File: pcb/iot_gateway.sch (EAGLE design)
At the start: 183 parts, among them CON1 LiPo Battery, J2 DC-JACK, Q1 AO3401, Q2 AO3401, Q3 AO3400, Q4 AO3400, T1 BC817-25, T2 BC817-25, T3 BC817-25, T4 BC817-25, T5 BC817-25, U1 EFM32GG11B4XX_Q100, U10 CCS811, U11 MIC4682, U12 MIC4682, U13 MIC39101, U14 FS312F-G, U15 TP4056, U16 FS8205, U17 ER-TFT035-6, U2 SST26VF064B, U3 SST26VF016B, U4 ESP8266EX, U5 RFM69HW, U6 SIM800C, U7 SI7021, U8 SI7210, U9 BMP280, X1 BM06B-SRSS-TB, X2 BM06B-SRSS-TB, Y1 8 MHz, Y2 32.768 kHz, Y3 24 MHz

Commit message: Change libs to new scheme
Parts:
- removed A1, A2, A3, A4: U.FL, SparkFun:U.FL
- removed J1: (no value), SparkFun-Connectors:SIMHOLDERSIM
- removed X1, X2: BM06B-SRSS-TB, con-jst2:BM06B-SRSS-TB
- added CON2: 6P-SH-TOP, JST:6P-SH-TOP
- added CON3: 2P-PH-TOP, JST:2P-PH-TOP
- added RFCON1, RFCON2, RFCON3, RFCON4: RFCON-U.FL, RF Connector:RFCON-U.FL
- added SIM1: SIMHOLDER-SMD, SIM Holder:SIMHOLDER-SMD
- B1: value KLJ-1230 -> BUZZER-SMD; device muRata-piezo:PKLCS1212E2400-R1 -> Buzzer:BUZZER-SMD
- C1, C13, C14, C15, C16, C2, C21, C23, C28, C29, C3, C30, C31, C37, C38, C4, C43, C47, C49, C5, C50, C52, C53, C54, C6, C7: device Kemet_by_JSilva:C0603C104K4RACTU -> Capacitor:CAPACITOR-0603
- C10, C11, C9: device Kemet_by_JSilva:C0603C102J5GACTU -> Capacitor:CAPACITOR-0603
- C12, C22, C36, C42, C46, C48, C51: device SparkFun:CAP_POL1206-KIT -> Capacitor:TANTALUM-CAPACITOR-CASE-A-EIA3216
- C17: device Kemet_by_JSilva:C0603C100J5GACTU -> Capacitor:CAPACITOR-0603
- C18: device Kemet_by_JSilva:C0603C479C5GACTU -> Capacitor:CAPACITOR-0603
- C19, C20: device Kemet_by_JSilva:C0603C200J5GACTU -> Capacitor:CAPACITOR-0603
- C24: device Kemet_by_JSilva:C1206C107M9PACTU -> Capacitor:CAPACITOR-0603
- C25, C8: device Kemet_by_JSilva:C0603C105K9RACTU -> Capacitor:CAPACITOR-0603
- C26, C27: device Kemet_by_JSilva:C0603C330J5GACTU -> Capacitor:CAPACITOR-0603
- C32, C33: device Kemet_by_JSilva:C0603X104K5RACTU -> Capacitor:CAPACITOR-0603
- C34: value 470UF -> 470uF; device Panasonic-EEE0_EEE1_EEE2_EEEFC:EEE-1CA471UAP-CASE-F -> Capacitor:ALUMINIUM-CAPACITOR-CASE-F
- C35, C41, C44, C45: device Kemet_by_JSilva:C0603C471J5GACTU -> Capacitor:CAPACITOR-0603
- C39, C40: value 220UF -> 220uF; device Panasonic-EEE0_EEE1_EEE2_EEEFC:EEE-0JA221WP-CASE-D -> Capacitor:ALUMINIUM-CAPACITOR-CASE-D
- CON1: value LiPo Battery -> 6P-SH-TOP; device JST_PH_SMD:JST_PH_SMD_2 -> JST:6P-SH-TOP; MF JST (JAPAN SOLDERLESS TERMINALS) -> (none); MPN B2B-PH-SM4-TB(LF)(SN) -> (none); OC_NEWARK unknown -> (none)
- D1: device SparkFun-LED:WS2812B -> LED:WS2812B-SMD
- D2: device ATWINC1500:LED1206 -> LED:LED1206
- D3: device smaj_10:SMAJ12A -> TVS:SMAJ12A
- D4, D5: device diodes:SK54L -> Generic Diode:SK54L
- D6, D7: device diodes:DSK24 -> Generic Diode:DSK24
- E1, E2: value ANTENNATRACE-15.2MM -> 2.4GHZTRACE-15.2MM; device esp8266-development-board:ANTENNATRACE-15.2MM -> Microstrip Antenna:2.4GHZTRACE-15.2MM
- J2: value DC-JACK -> DCJACK-SMD; device dc-jack-smd:DC-JACK -> DC Jack:DCJACK-SMD
- L1: device microbuilder 2:INDUCTOR0603 -> Inductor:INDUCTOR-0603
- L2, L3: device Inductor:SLH1207S680MTT -> Inductor:INDUCTOR-12X12X7MM
- R1, R17, R18, R2, R20, R21, R22, R24, R28, R31, R32, R33, R36, R37, R4, R40, R43, R50, R53, R6, R67, R7: device Vishay_by_JSilva:CRCW060310K0FKEA -> Resistor:RESISTOR-0603
- R10, R11, R9: device Vishay_by_JSilva:CRCW06031M00FKEA -> Resistor:RESISTOR-0603
- R12, R13, R14, R59: device Vishay_by_JSilva:CRCW0603100RFKEA -> Resistor:RESISTOR-0603
- R15, R25, R38, R41, R5, R51, R52, R54, R56, R57, R60, R61, R66, R8: device Vishay_by_JSilva:CRCW0603100KFKEA -> Resistor:RESISTOR-0603
- R16, R34, R35, R64, R65: device Vishay_by_JSilva:CRCW06030000Z0EA -> Resistor:RESISTOR-0603
- R19: device Vishay_by_JSilva:CRCW060312K0FKEA -> Resistor:RESISTOR-0603
- R23: device Vishay_by_JSilva:CRCW0603200RFKEA -> Resistor:RESISTOR-0603
- R26, R27, R29: device Vishay_by_JSilva:CRCW060322R0FKEA -> Resistor:RESISTOR-0603
- R3, R58, R68: device Vishay_by_JSilva:CRCW06031K00FKEA -> Resistor:RESISTOR-0603
- R30: device Vishay_by_JSilva:CRCW0603330RFKEA -> Resistor:RESISTOR-0603
- R39, R42, R63: device Vishay_by_JSilva:CRCW060310M0JNEA -> Resistor:RESISTOR-0603
- R44, R48: device Vishay_by_JSilva:CRCW06033K01FKEA -> Resistor:RESISTOR-0603
- R45: device Vishay_by_JSilva:CRCW0603953RFKEA -> Resistor:RESISTOR-0603
- R46: device Vishay_by_JSilva:CRCW0603300KFKEA -> Resistor:RESISTOR-0603
- R47, R55: device Vishay_by_JSilva:CRCW060347K0FKEA -> Resistor:RESISTOR-0603
- R49: device Vishay_by_JSilva:CRCW06031K20FKEA -> Resistor:RESISTOR-0603
- R62: device Vishay_by_JSilva:CRCW06031K50FKEA -> Resistor:RESISTOR-0603
- S1: device Switches:TAC_SWITCHSMD -> Switch:TAC_SWITCHSMD
- S2, S3, S4: device Switches:TAC_SWITCHSMD_4.5X4.5 -> Switch:TAC_SWITCHSMD_4.5X4.5
- T1, T2, T3, T4, T5: value BC817-25 -> BC817; device BC817:BC817-25 -> Generic BJT:BC817; MPN BC81725 -> (none); OC_NEWARK 04X5937 -> (none)
- TP1, TP2, TP3, TP4, TP5: value TPB1,27 -> TESTPOINT; device ReflowController:TPB1,27 -> PADs:TESTPOINT
- U14: device buckboost:FS312F-G -> Fortune:FS312F-G
- U16: device buckboost:FS8205 -> Fortune:FS8205
- U4: device ESP8266EX:ESP8266EX -> Espressif:ESP8266EX
- Y1, Y3: device crystal2:NX5032GA -> Crystal:CRYSTAL2-SMD-5X3
- Y2: device crystal2:CRYTALCM200S -> Crystal:CRYSTALCM2000S
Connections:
- net !RESET: now also CON1-2.S; no longer X1-2.S
- net !WIFI_RST: now also CON2-1.S; no longer X2-1.S
- net 3V3: now also B1.+, CON1-1.S; no longer B1.A, X1-1.S
- net 5V0: now also C40.+; no longer C40.1
- net GBAT: now also CON3-2.S; no longer CON1.2
- net GND: now also C34.-, C39.-, C40.-, CON1-6.S, CON2-6.S, RFCON1.GND, RFCON2.GND, RFCON3.GND, RFCON4.GND, SIM1.GND; no longer A1.GND@0, A1.GND@1, A2.GND@0, A2.GND@1, A3.GND@0, A3.GND@1, A4.GND@0, A4.GND@1, C34.2, C39.2, C40.2, J1.GND, X1-6.S, X2-6.S
- net N$10: now also RFCON1.SIGNAL; no longer A1.SIGNAL
- net N$18: now also SIM1.CLK; no longer J1.CLK
- net N$2: now also RFCON4.SIGNAL; no longer A4.SIGNAL
- net N$22: now also RFCON3.SIGNAL; no longer A3.SIGNAL
- net N$3: now also SIM1.RST; no longer J1.RST
- net N$35: now also B1.-; no longer B1.B
- net N$39: now also SIM1.DATA; no longer J1.I/O
- net N$43: now also C39.+; no longer C39.1
- net N$45: now also RFCON2.SIGNAL; no longer A2.SIGNAL
- net SIM_VDD: now also SIM1.VCC; no longer J1.VCC
- net SWCLK: now also CON1-3.S; no longer X1-3.S
- net SWDIO: now also CON1-4.S; no longer X1-4.S
- net SWO: now also CON1-5.S; no longer X1-5.S
- net VBAT: now also CON3-1.S; no longer CON1.1
- net VIN: now also C34.+; no longer C34.1
- net WIFI_BOOT: now also CON2-2.S; no longer X2-2.S
- net WIFI_RX_FW: now also CON2-4.S; no longer X2-4.S
- net WIFI_TX_DBG: now also CON2-5.S; no longer X2-5.S
- net WIFI_TX_FW: now also CON2-3.S; no longer X2-3.S
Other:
- note added: "Option 2: L1: 5.6pF capacitor C17: Do not place C18: Do not place"
- note removed: "Option 2: L2: 5.6pF capacitor C15: Do not place C21: Do not place"

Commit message: Update libraries
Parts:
- C24: device Capacitor:CAPACITOR-0603 -> Capacitor:CAPACITOR-1206
- D1: device LED:WS2812B-SMD -> LED:WS2812B-SMD5050
- D4, D5: OCLCSC C129854 -> C129816
- R28, R30, R31, R32, R33: MF VISHAY -> (none)
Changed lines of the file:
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@@
 <?xml version="1.0" encoding="utf-8"?>
 <!DOCTYPE eagle SYSTEM "eagle.dtd">
-<eagle version="9.3.2">
+<eagle version="9.3.0">
 <drawing>
 <settings>
@@
 <part name="GND47" library="Supply Symbol" deviceset="GND" device=""/>
 <part name="R35" library="Resistor" deviceset="RESISTOR" device="-0603" value="0 Ohms"/>
-<part name="C24" library="Capacitor" deviceset="CAPACITOR" device="-0603" value="100uF"/>
+<part name="C24" library="Capacitor" deviceset="CAPACITOR" device="-1206" value="100uF"/>
 <part name="GND42" library="Supply Symbol" deviceset="GND" device=""/>
 <part name="4V23" library="Supply Symbol" deviceset="4V2" device="" value="4V2"/>
@@
 <attribute name="MF" value="FAIRCHILD SEMICONDUCTOR"/>
 </part>
-<part name="R30" library="Resistor" deviceset="RESISTOR" device="-0603" value="330 Ohms">
-<attribute name="MF" value="VISHAY"/>
-</part>
-<part name="R32" library="Resistor" deviceset="RESISTOR" device="-0603" value="10K Ohms">
-<attribute name="MF" value="VISHAY"/>
-</part>
-<part name="R28" library="Resistor" deviceset="RESISTOR" device="-0603" value="10K Ohms">
-<attribute name="MF" value="VISHAY"/>
-</part>
-<part name="R31" library="Resistor" deviceset="RESISTOR" device="-0603" value="10K Ohms">
-<attribute name="MF" value="VISHAY"/>
-</part>
+<part name="R30" library="Resistor" deviceset="RESISTOR" device="-0603" value="330 Ohms"/>
+<part name="R32" library="Resistor" deviceset="RESISTOR" device="-0603" value="10K Ohms"/>
+<part name="R28" library="Resistor" deviceset="RESISTOR" device="-0603" value="10K Ohms"/>
+<part name="R31" library="Resistor" deviceset="RESISTOR" device="-0603" value="10K Ohms"/>
 <part name="D2" library="LED" deviceset="LED" device="1206" value="RED"/>
 <part name="C25" library="Capacitor" deviceset="CAPACITOR" device="-0603" value="1uF"/>
@@
 <attribute name="MF" value="FAIRCHILD SEMICONDUCTOR"/>
 </part>
-<part name="R33" library="Resistor" deviceset="RESISTOR" device="-0603" value="10K Ohms">
-<attribute name="MF" value="VISHAY"/>
-</part>
+<part name="R33" library="Resistor" deviceset="RESISTOR" device="-0603" value="10K Ohms"/>
 <part name="GND46" library="Supply Symbol" deviceset="GND" device=""/>
 <part name="4V24" library="Supply Symbol" deviceset="4V2" device="" value="4V2"/>
@@
 <part name="D6" library="Generic Diode" deviceset="DSK24" device="" value="DSK24"/>
 <part name="D4" library="Generic Diode" deviceset="SK54L" device="" value="SK54L">
-<attribute name="OCLCSC" value="C129854"/>
+<attribute name="OCLCSC" value="C129816"/>
 </part>
 <part name="C32" library="Capacitor" deviceset="CAPACITOR" device="-0603" value="100nF"/>
@@
 <part name="VBAT1" library="Supply Symbol" deviceset="VBAT" device=""/>
 <part name="D5" library="Generic Diode" deviceset="SK54L" device="" value="SK54L">
-<attribute name="OCLCSC" value="C129854"/>
+<attribute name="OCLCSC" value="C129816"/>
 </part>
 <part name="C33" library="Capacitor" deviceset="CAPACITOR" device="-0603" value="100nF"/>
@@
 <part name="GND99" library="Supply Symbol" deviceset="GND" device=""/>
 <part name="J2" library="DC Jack" deviceset="DCJACK" device="-SMD"/>
-<part name="D1" library="LED" deviceset="WS2812B" device="-SMD" value="WS2812B"/>
+<part name="D1" library="LED" deviceset="WS2812B" device="-SMD5050" value="WS2812B"/>
 <part name="GND10" library="Supply Symbol" deviceset="GND" device=""/>
 <part name="C7" library="Capacitor" deviceset="CAPACITOR" device="-0603" value="100nF"/>
@@
 </instance>
 <instance part="R30" gate="G$1" x="96.52" y="157.48" smashed="yes" rot="R90">
-<attribute name="MF" x="96.52" y="157.48" size="1.778" layer="96" rot="R90" display="off"/>
 <attribute name="VALUE" x="100.1776" y="158.1658" size="1.778" layer="96" ratio="10" rot="SR90"/>
 <attribute name="NAME" x="93.7514" y="158.4706" size="1.778" layer="95" ratio="10" rot="SR90"/>
 </instance>
 <instance part="R32" gate="G$1" x="111.76" y="147.32" smashed="yes">
-<attribute name="MF" x="111.76" y="147.32" size="1.778" layer="96" rot="R180" display="off"/>
 <attribute name="VALUE" x="112.4458" y="143.6624" size="1.778" layer="96" ratio="10" rot="SR0"/>
 <attribute name="NAME" x="112.7506" y="150.0886" size="1.778" layer="95" ratio="10" rot="SR0"/>
 </instance>
 <instance part="R28" gate="G$1" x="73.66" y="114.3" smashed="yes">
-<attribute name="MF" x="73.66" y="114.3" size="1.778" layer="96" rot="R180" display="off"/>
 <attribute name="VALUE" x="74.3458" y="110.6424" size="1.778" layer="96" ratio="10" rot="SR0"/>
 <attribute name="NAME" x="74.6506" y="117.0686" size="1.778" layer="95" ratio="10" rot="SR0"/>
 </instance>
 <instance part="R31" gate="G$1" x="106.68" y="142.24" smashed="yes" rot="R270">
-<attribute name="MF" x="106.68" y="142.24" size="1.778" layer="96" rot="R90" display="off"/>
 <attribute name="VALUE" x="103.0224" y="141.5542" size="1.778" layer="96" ratio="10" rot="SR270"/>
 <attribute name="NAME" x="109.4486" y="141.2494" size="1.778" layer="95" ratio="10" rot="SR270"/>
@@
 </instance>
 <instance part="R33" gate="G$1" x="147.32" y="177.8" smashed="yes">
-<attribute name="MF" x="147.32" y="177.8" size="1.778" layer="96" rot="R180" display="off"/>
 <attribute name="VALUE" x="148.0058" y="174.1424" size="1.778" layer="96" ratio="10" rot="SR0"/>
 <attribute name="NAME" x="148.3106" y="180.5686" size="1.778" layer="95" ratio="10" rot="SR0"/>

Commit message: Final board ordered
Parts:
- added U$1: GECKO, Silkscreen:GECKO
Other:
- moved on the sheet: R8, U2

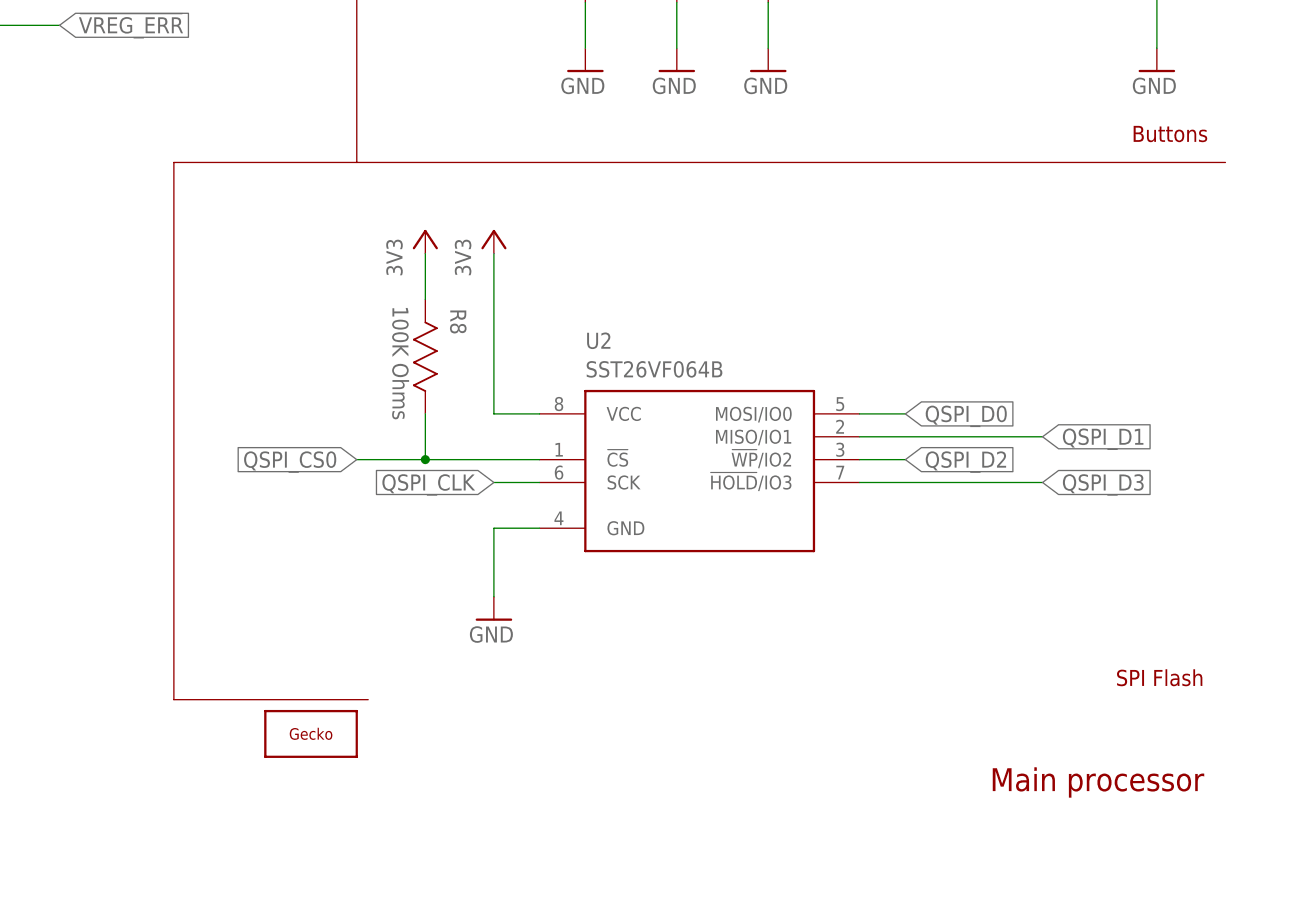
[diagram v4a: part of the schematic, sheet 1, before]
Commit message: Change gateway sch frame
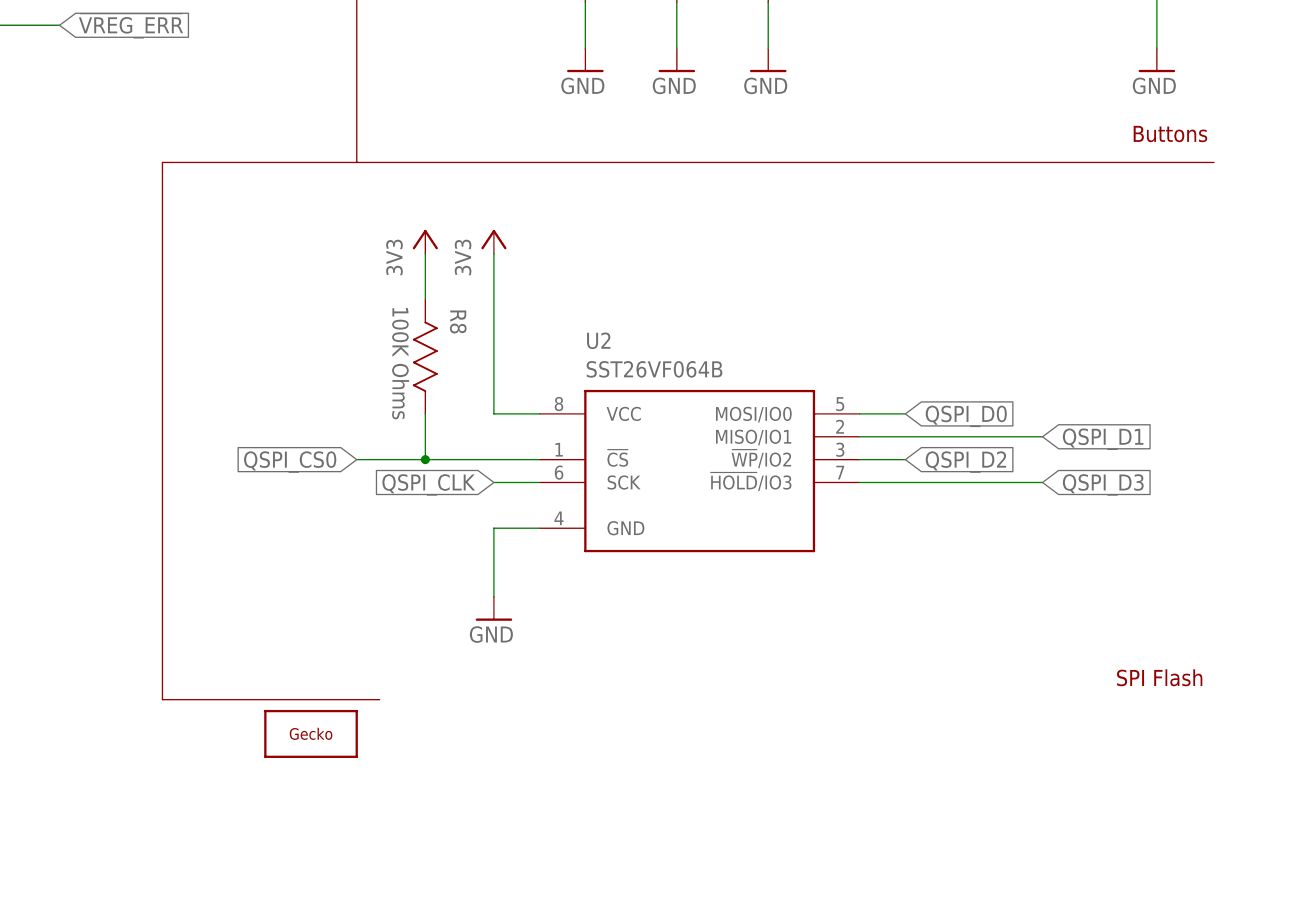
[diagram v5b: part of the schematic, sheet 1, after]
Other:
- note removed: "Main processor"
- note removed: "Wifi access"

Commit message: Fix hardware errors
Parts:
- removed T2: BC817, Generic BJT:BC817
- added Q5: AO3400, Alpha Omega:AO3400
- added SJ1: (no value), Solder Jumper:SJS
- R2: value 10K Ohms -> 22 Ohms
- R5: value 100K Ohms -> 1K Ohms
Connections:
- new net N$11: SJ1.1, U4.XPD_DCDC/IO16
- net !WIFI_RST: now also SJ1.2; no longer U4.XPD_DCDC/IO16
- net GND: now also J2.2, Q5.S; no longer J2.3, T2.E
- net N$19: now also Q5.D; no longer T2.C
- net N$32: now also Q5.G; no longer T2.B
- net VIN_DET: now also J2.3; no longer J2.2
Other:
- moved on the sheet: D1, R21, R5
